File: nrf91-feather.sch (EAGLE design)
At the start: 93 parts, among them J2 CON-HEADER-1X12-MALE-PIN, J3 CON-HEADER-1X16-MALE-PIN, J4 CON-1909763-1, J5 CON-SIM-104224-0820, J6 CON-S2B-PH-SM4-TB(LF)(SN), J7 CON-1909763-1, J8 CON-USB-DX07S016JA1R1500, J9 CON-TC2030-MCP-NL, Q1 MOSFET-N-SC89, Q2 MOSFET-DUAL-COMP-SOT563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

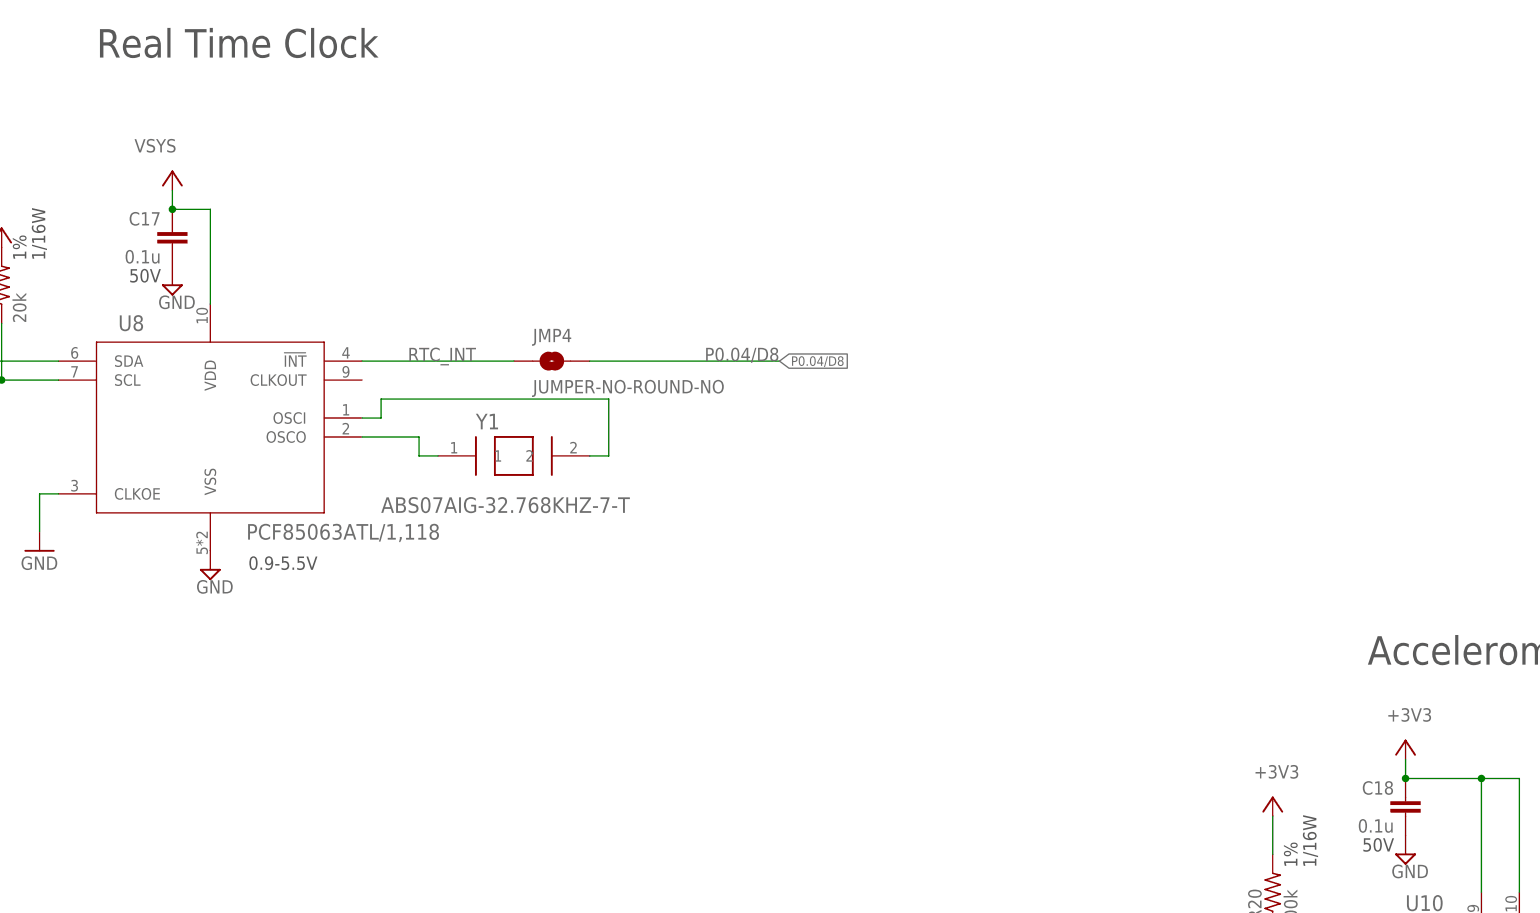
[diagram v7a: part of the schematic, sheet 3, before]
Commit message: Fixed Iq issues when Vbat > 3.8V
Changed:

Connected RTC directly to 3.3V
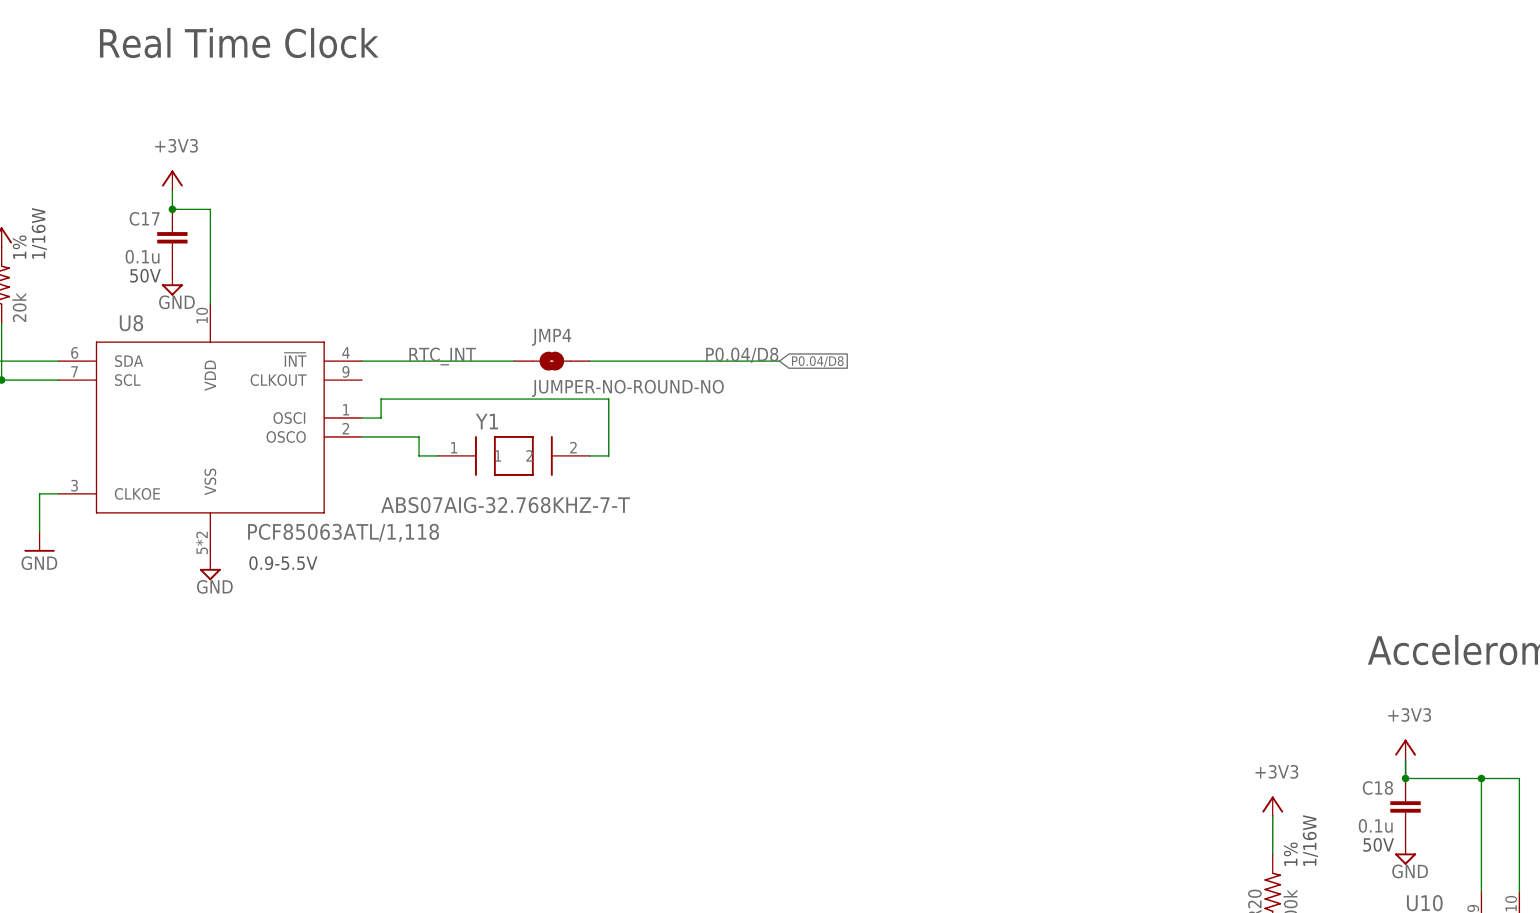
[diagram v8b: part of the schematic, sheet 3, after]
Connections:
- net +3V3: now also C17.1, U8.VDD
- net VSYS: no longer C17.1, U8.VDD
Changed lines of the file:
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@@
 <part name="+3V4" library="supply1" library_urn="urn:adsk.eagle:library:371" deviceset="+3V3" device=""/>
 <part name="+3V9" library="supply1" library_urn="urn:adsk.eagle:library:371" deviceset="+3V3" device=""/>
-<part name="P+9" library="wolff-den" library_urn="urn:adsk.eagle:library:6370453" deviceset="VSYS" device=""/>
 <part name="R17" library="wolff-den" library_urn="urn:adsk.eagle:library:6370453" deviceset="RES" device="-0402" package3d_urn="urn:adsk.eagle:package:19061974/5" technology="-20K-1%" value="20k"/>
 <part name="R18" library="wolff-den" library_urn="urn:adsk.eagle:library:6370453" deviceset="RES" device="-0402" package3d_urn="urn:adsk.eagle:package:19061974/5" technology="-20K-1%" value="20k"/>
@@
 <part name="R24" library="wolff-den" library_urn="urn:adsk.eagle:library:6370453" deviceset="RES" device="-0402" package3d_urn="urn:adsk.eagle:package:19061974/5" technology="-100K-1%" value="100k"/>
 <part name="GND48" library="supply1" library_urn="urn:adsk.eagle:library:371" deviceset="GND" device=""/>
+<part name="+3V8" library="supply1" library_urn="urn:adsk.eagle:library:371" deviceset="+3V3" device=""/>
 </parts>
 <sheets>
@@
 <attribute name="VALUE" x="104.14" y="195.58" size="1.778" layer="96" rot="R90"/>
 </instance>
-<instance part="P+9" gate="G$2" x="129.54" y="208.28" smashed="yes">
-<attribute name="VALUE" x="124.46" y="210.82" size="1.778" layer="96"/>
-</instance>
 <instance part="R17" gate="G$1" x="96.52" y="193.04" smashed="yes" rot="R90">
 <attribute name="NAME" x="95.0214" y="189.23" size="1.778" layer="95" rot="R90"/>
@@
 <attribute name="VALUE" x="177.8" y="180.34" size="1.778" layer="96" font="vector" align="top-left"/>
 </instance>
+<instance part="+3V8" gate="G$1" x="129.54" y="208.28" smashed="yes">
+<attribute name="VALUE" x="127" y="210.82" size="1.778" layer="96"/>
+</instance>
 </instances>
 <busses>
@@
 <wire x1="294.64" y1="127" x2="294.64" y2="129.54" width="0.1524" layer="91"/>
 <junction x="294.64" y="127"/>
+<wire x1="294.64" y1="127" x2="294.64" y2="129.54" width="0.1524" layer="91"/>
 </segment>
 <segment>
@@
 <wire x1="276.86" y1="116.84" x2="276.86" y2="121.92" width="0.1524" layer="91"/>
 </segment>
-</net>
-<net name="VSYS" class="0">
 <segment>
 <pinref part="C17" gate="A" pin="1"/>
@@
 <pinref part="U8" gate="A" pin="VDD"/>
 <wire x1="134.62" y1="203.2" x2="134.62" y2="190.5" width="0.1524" layer="91"/>
-<pinref part="P+9" gate="G$2" pin="VSYS"/>
+<pinref part="+3V8" gate="G$1" pin="+3V3"/>
 </segment>
 </net>
